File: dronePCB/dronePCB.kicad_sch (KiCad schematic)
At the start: 63 parts, among them IC3 DPS368XTSA1, IC4 ICM-42688-P, J10 DVR, J11 Strobe top, J12 Strobe bottom, J13 ToF400C, J14 ToF400C, J15 ToF400C, J16 ToF400C, J17 ToF400C, J6 Camera, J7 VID_ANT, J8 GEP-M10Q, J9 Avatar GMx, Q1 BSS138, Q2 BSS138, U10 TF-01A, U7 E28-2G4M12SX, U8 AT7456E, U9 TX5823, Y2 27MHz

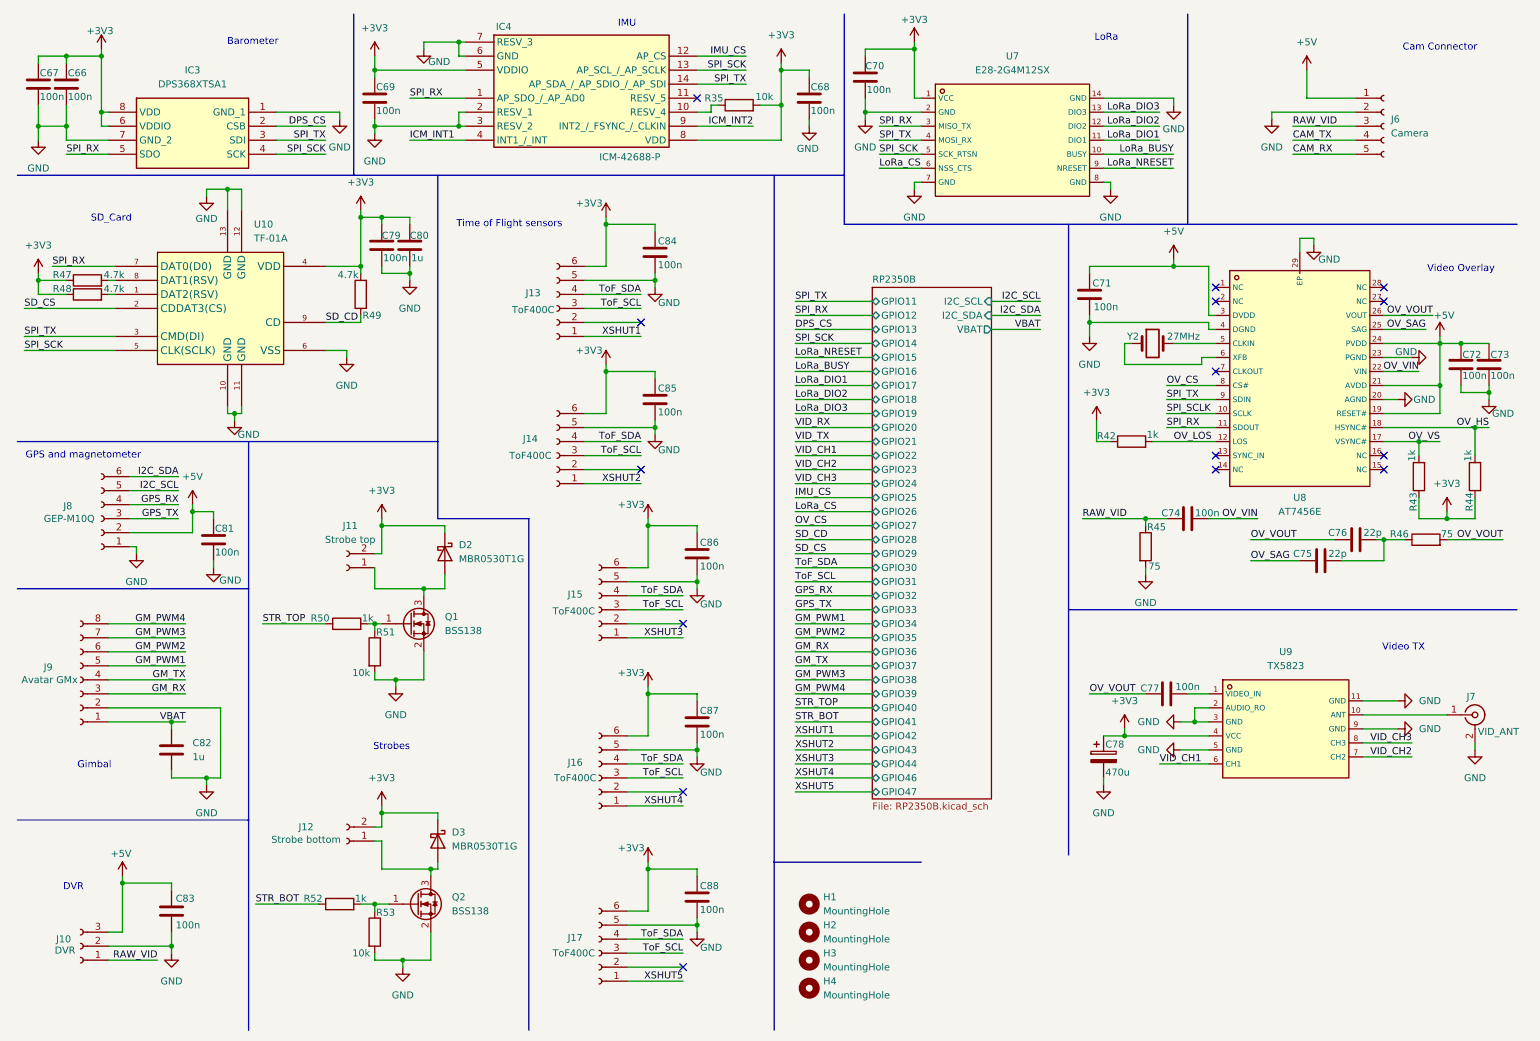
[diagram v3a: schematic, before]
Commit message: Routed RP2350B w/ dependencies + power circuit
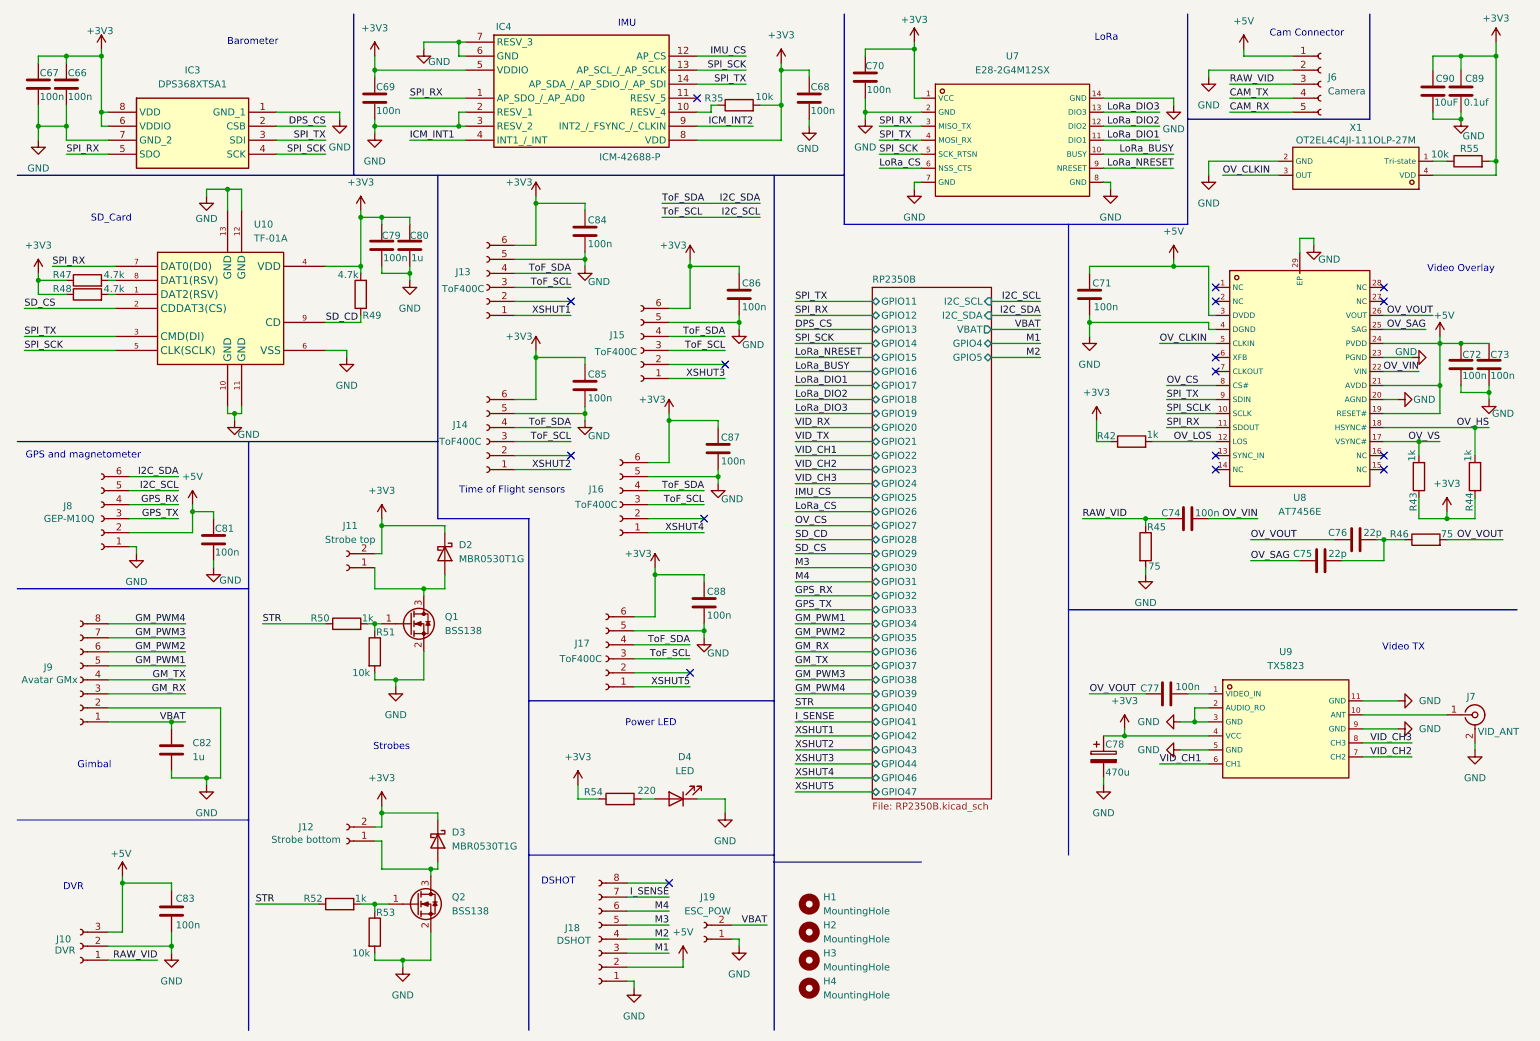
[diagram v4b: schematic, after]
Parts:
- removed Y2: 27MHz, symbol Device:Crystal
- added C89: 0.1uf, Capacitor_SMD:C_0805_2012Metric_Pad1.18x1.45mm_HandSolder, symbol Device:C
- added C90: 10uF, Capacitor_SMD:C_0805_2012Metric_Pad1.18x1.45mm_HandSolder, symbol Device:C
- added D4: LED, LED_SMD:LED_0201_0603Metric_Pad0.64x0.40mm_HandSolder, symbol Device:LED
- added J18: DSHOT, Connector_JST:JST_PH_S8B-PH-SM4-TB_1x08-1MP_P2.00mm_Horizontal, symbol Connector:Conn_01x08_Socket
- added J19: ESC_POW, Connector_AMASS:AMASS_XT30U-F_1x02_P5.0mm_Vertical, symbol Connector:Conn_01x02_Socket
- added R54: 220, Capacitor_SMD:C_0805_2012Metric_Pad1.18x1.45mm_HandSolder, symbol Device:R
- added R55: 10k, Resistor_SMD:R_0805_2012Metric_Pad1.20x1.40mm_HandSolder, symbol Device:R
- added X1: OT2EL4C4JI-111OLP-27M, droneParts:OT2EL4C4JI-111OLP-27M, symbol OT2EL4C4JI-111OLP-27M:OT2EL4C4JI-111OLP-27M
- C66, C67, C68, C69, C70, C71, C72, C73, C74, C75, C76, C77, C78, C79, C80, C81, C82, C83, C84, C85, C86, C87, C88, R35, R42, R43, R44, R45, R46, R47, R48, R49, R50, R51, R52, R53: footprint (none) -> Capacitor_SMD:C_0805_2012Metric_Pad1.18x1.45mm_HandSolder
- H1, H2, H3, H4: footprint (none) -> MountingHole:MountingHole_2.2mm_M2
- IC3: footprint DPS368XTSA1 -> droneParts:DPS368XTSA1
- IC4: footprint IIM42352 -> droneParts:IIM42352
- J10: footprint (none) -> Connector_JST:JST_PH_S3B-PH-SM4-TB_1x03-1MP_P2.00mm_Horizontal
- J11, J12: footprint (none) -> Connector_JST:JST_PH_S2B-PH-SM4-TB_1x02-1MP_P2.00mm_Horizontal
- J13, J14, J15, J16, J17: footprint (none) -> Connector_JST:JST_PH_S6B-PH-SM4-TB_1x06-1MP_P2.00mm_Horizontal
- J6: footprint (none) -> Connector_JST:JST_PH_B5B-PH-SM4-TB_1x05-1MP_P2.00mm_Vertical
- J7: footprint (none) -> Connector_Coaxial:SMA_Amphenol_132134-11_Vertical
- J8: footprint (none) -> Connector_JST:JST_PH_B6B-PH-SM4-TB_1x06-1MP_P2.00mm_Vertical
- J9: footprint (none) -> Connector_JST:JST_PH_S8B-PH-SM4-TB_1x08-1MP_P2.00mm_Horizontal
- U10: footprint footprint:TF-SMD_TF-01A -> droneParts:TF-01A
- U7: footprint footprint:COMM-SMD_E28-2G4M12SX -> droneParts:COMM-SMD_E28-2G4M12SX
- U8: footprint footprint:TSSOP-28_L9.7-W4.4-P0.65-LS6.4-BL-EP-2 -> droneParts:AT7456E
- U9: footprint footprint:COMM-SMD_L22.2-W19.0-P2.54_TX5823 -> droneParts:TX5823
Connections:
- net STR_TOP is gone; now on net STR: R50.1
- net ToF_SCL is gone; now on net I2C_SCL: J13.3 (Pin_3), J14.3 (Pin_3), J15.3 (Pin_3), J16.3 (Pin_3), J17.3 (Pin_3)
- net ToF_SDA is gone; now on net I2C_SDA: J13.4 (Pin_4), J14.4 (Pin_4), J15.4 (Pin_4), J16.4 (Pin_4), J17.4 (Pin_4)
- net +3V3: now also C89.1, C90.1, R54.1, R55.2, X1.4 (VDD)
- net +5V: now also J18.2 (Pin_2)
- net GND: now also C89.2, C90.2, D4.1 (K), J18.1 (Pin_1), J19.1 (Pin_1), X1.2 (GND)
- net VBAT: now also J19.2 (Pin_2)
- net OV_CLKIN: now reaches U8.5 (CLKIN)
- net OV_CLKIN: now also X1.3 (OUT)
- net STR_BOT renamed STR
- new net: R55.1, X1.1 (Tri-state)
- new net: D4.2 (A), R54.2
- new net I_SENSE: J18.7 (Pin_7)
- new net M1: J18.3 (Pin_3)
- new net M2: J18.4 (Pin_4)
- new net M3: J18.5 (Pin_5)
- new net M4: J18.6 (Pin_6)
- no-connect marks 15 -> 17
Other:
- sheet RP2350B ports: added GPIO4, GPIO5; removed none
- note added: "DSHOT"
- note added: "Power LED"
- moved on the sheet: C84, C85, C86, C87, C88, J13, J14, J15, J16, J17, J6

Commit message: Finished PCB
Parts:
- added SW4, SW5, SW6: CJS-1200TB1, droneParts:CJS1200TB1, symbol CJS-1200TB1:CJS-1200TB1
- C78: footprint Capacitor_SMD:C_0805_2012Metric_Pad1.18x1.45mm_HandSolder -> Capacitor_SMD:C_Elec_3x5.4
- D4: footprint LED_SMD:LED_0201_0603Metric_Pad0.64x0.40mm_HandSolder -> LED_SMD:LED_0805_2012Metric_Pad1.15x1.40mm_HandSolder
- J10: footprint Connector_JST:JST_PH_S3B-PH-SM4-TB_1x03-1MP_P2.00mm_Horizontal -> Connector_JST:JST_PH_B3B-PH-SM4-TB_1x03-1MP_P2.00mm_Vertical
- J11, J12: footprint Connector_JST:JST_PH_S2B-PH-SM4-TB_1x02-1MP_P2.00mm_Horizontal -> Connector_JST:JST_PH_B2B-PH-SM4-TB_1x02-1MP_P2.00mm_Vertical
- J13, J14, J15, J16, J17: footprint Connector_JST:JST_PH_S6B-PH-SM4-TB_1x06-1MP_P2.00mm_Horizontal -> Connector_JST:JST_PH_B6B-PH-SM4-TB_1x06-1MP_P2.00mm_Vertical
- J18, J9: footprint Connector_JST:JST_PH_S8B-PH-SM4-TB_1x08-1MP_P2.00mm_Horizontal -> Connector_JST:JST_PH_B8B-PH-SM4-TB_1x08-1MP_P2.00mm_Vertical
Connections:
- net SPI_SCLK is gone; now on net SPI_SCK: U8.10 (SCLK)
- net GND: now also SW4.2 (COM), SW5.2 (COM), SW6.2 (COM)
- net OV_VOUT: no longer C77.1, R46.2
- net STR: no longer R50.1
- net VID_CH1: now also SW6.1 (NO)
- net VID_CH2: now also SW4.1 (NO)
- net VID_CH3: now also SW5.1 (NO)
- new net OV_OUT: C77.1, R46.2
- new net STR_TOP: R50.1
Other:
- moved on the sheet: C77, C78, J7, U9
